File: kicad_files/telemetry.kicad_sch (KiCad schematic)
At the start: 24 parts, among them J3 RFD900ux 10 Pin Header, J4 Conn_ARM_JTAG_SWD_10, J5 RFD900ux 3 Pin Power Select, J6 USB_C_Receptacle_USB2.0_16P, U8 74LVC1G125, U9 WE-TVS-82400102

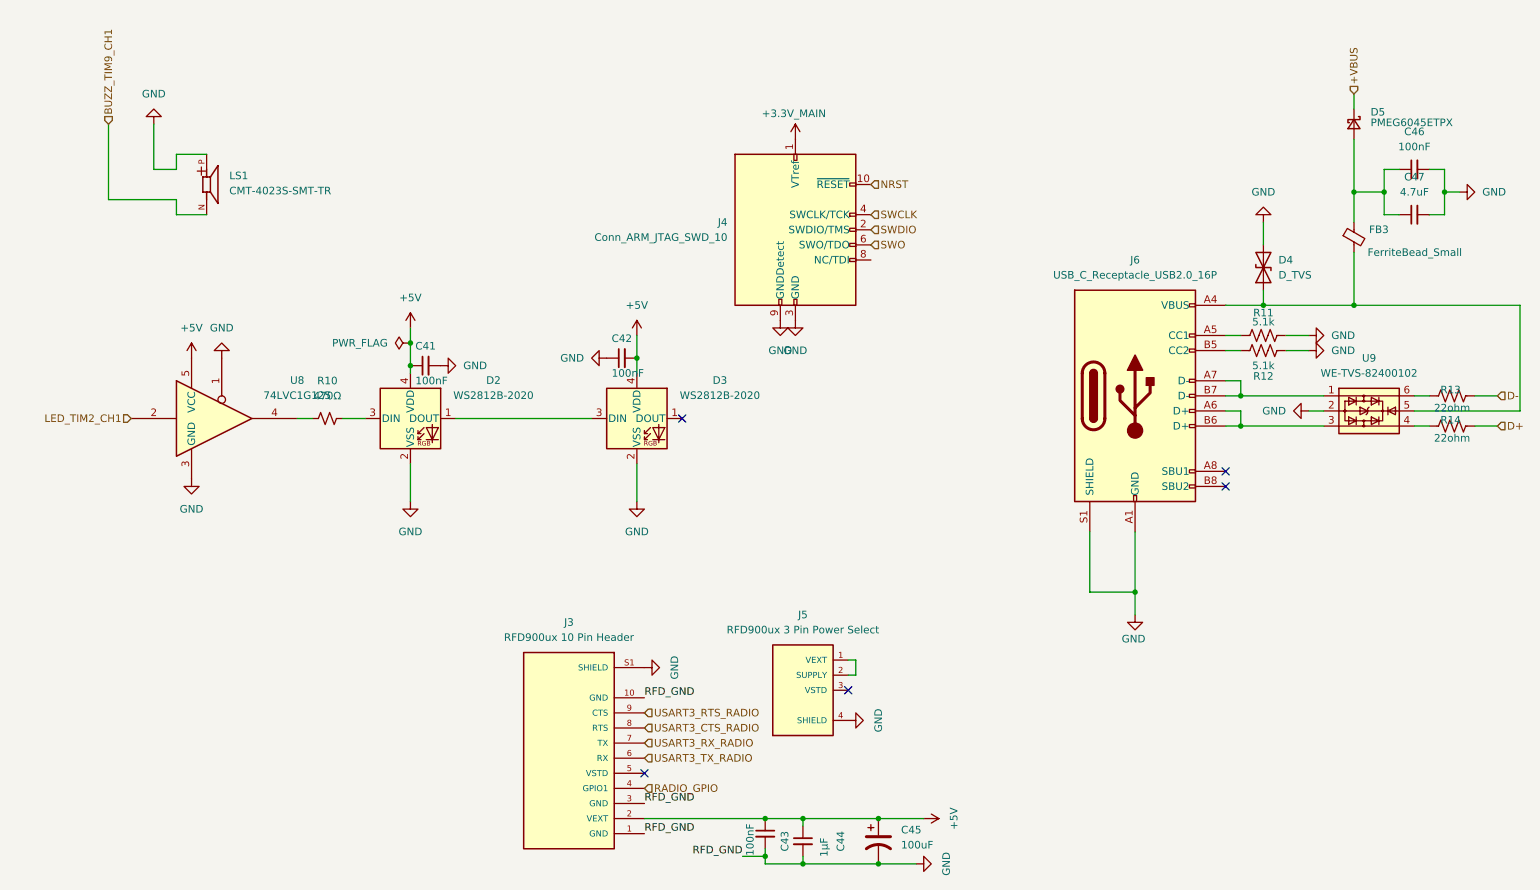
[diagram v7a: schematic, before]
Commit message: size polyfuse, final drc stuff
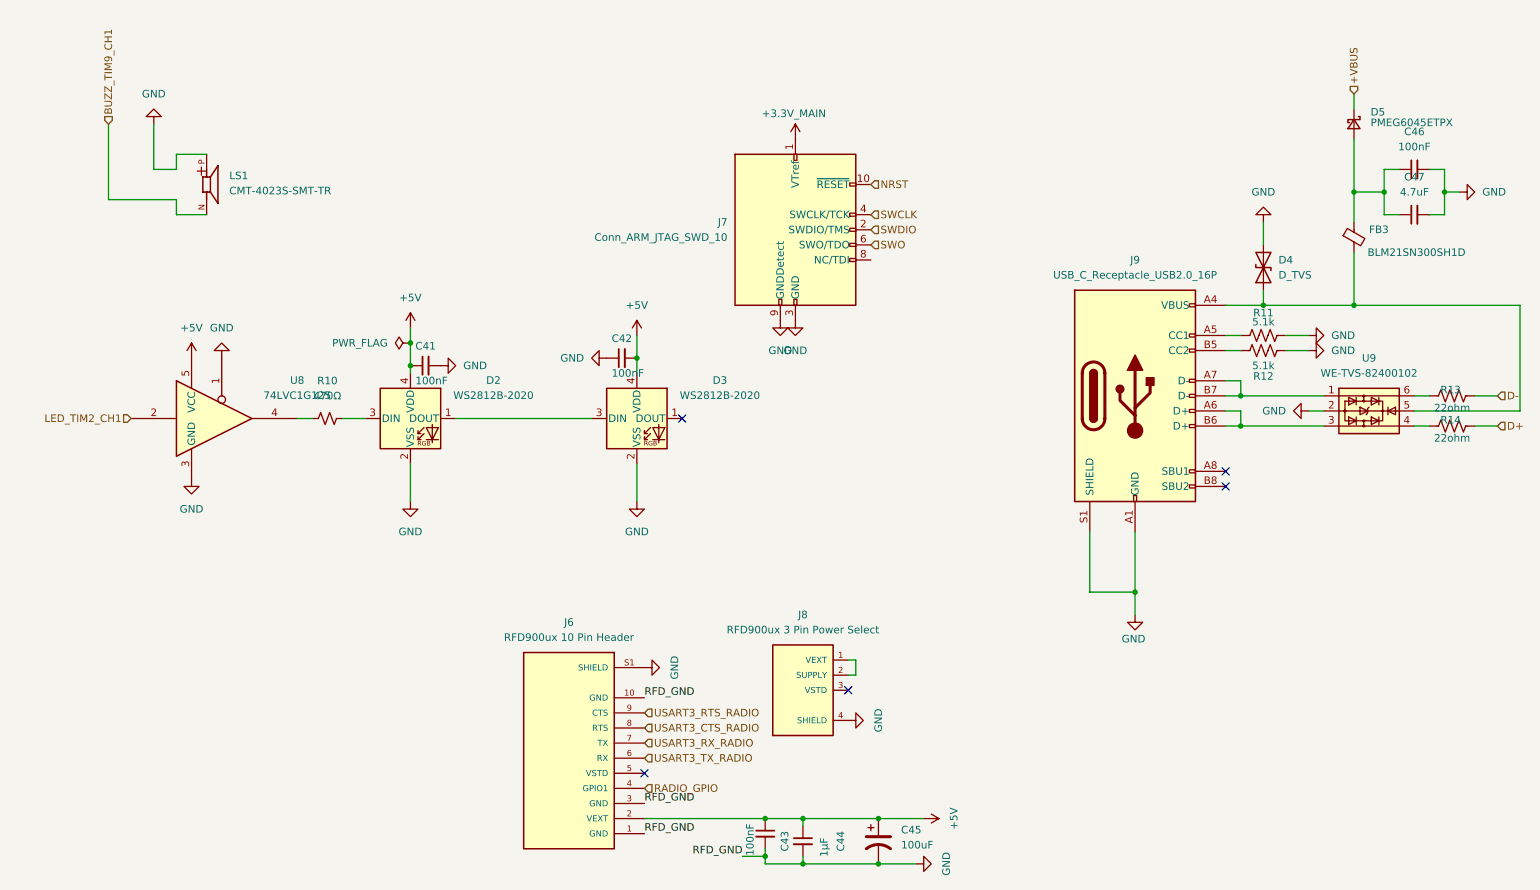
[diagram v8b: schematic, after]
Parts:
- FB3: value FerriteBead_Small -> BLM21SN300SH1D; footprint Resistor_SMD:R_0805_2012Metric -> Inductor_SMD:L_0805_2012Metric
- renumbered J3 to J6, J4 to J7, J5 to J8, J6 to J9
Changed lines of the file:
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@@
 			)
 		)
-		(property "Value" "FerriteBead_Small"
+		(property "Value" "BLM21SN300SH1D"
 			(at 241.046 58.42 0)
 			(show_name no)
@@
 			)
 		)
-		(property "Footprint" "Resistor_SMD:R_0805_2012Metric"
+		(property "Footprint" "Inductor_SMD:L_0805_2012Metric"
 			(at 236.982 55.88 90)
 			(hide yes)
@@
 		(dnp no)
 		(fields_autoplaced yes)
-		(property "Reference" "J3"
+		(property "Reference" "J6"
 			(at 106.68 120.65 0)
 			(show_name no)
@@
 			(project "versorlite"
 				(path "/1a230af0-0a74-48f7-8607-b087121dda49/4d884b5c-b332-4347-90a4-1c2e65497882"
-					(reference "J3")
+					(reference "J6")
 					(unit 1)
 				)
@@
 		(dnp no)
 		(fields_autoplaced yes)
-		(property "Reference" "J5"
+		(property "Reference" "J8"
 			(at 146.05 119.38 0)
 			(show_name no)
@@
 			(project "versorlite"
 				(path "/1a230af0-0a74-48f7-8607-b087121dda49/4d884b5c-b332-4347-90a4-1c2e65497882"
-					(reference "J5")
+					(reference "J8")
 					(unit 1)
 				)
@@
 		(dnp no)
 		(fields_autoplaced yes)
-		(property "Reference" "J6"
+		(property "Reference" "J9"
 			(at 201.93 59.69 0)
 			(show_name no)
@@
 			(project "versorlite"
 				(path "/1a230af0-0a74-48f7-8607-b087121dda49/4d884b5c-b332-4347-90a4-1c2e65497882"
-					(reference "J6")
+					(reference "J9")
 					(unit 1)
 				)
@@
 		(dnp no)
 		(fields_autoplaced yes)
-		(property "Reference" "J4"
+		(property "Reference" "J7"
 			(at 133.35 53.3399 0)
 			(show_name no)
@@
 			(project "versorlite"
 				(path "/1a230af0-0a74-48f7-8607-b087121dda49/4d884b5c-b332-4347-90a4-1c2e65497882"
-					(reference "J4")
+					(reference "J7")
 					(unit 1)
 				)
